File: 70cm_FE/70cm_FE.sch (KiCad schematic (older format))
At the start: 142 parts, among them J2 U.FL, J3 U.FL, J4 U.FL, Q1 2SC3356, Q2 2SC3356, Q3 2SC3356, Q4 2N7002, U1 HT7533-1, U2 74HC14, U3 74HC14, U4 LM393, U5 M68710L

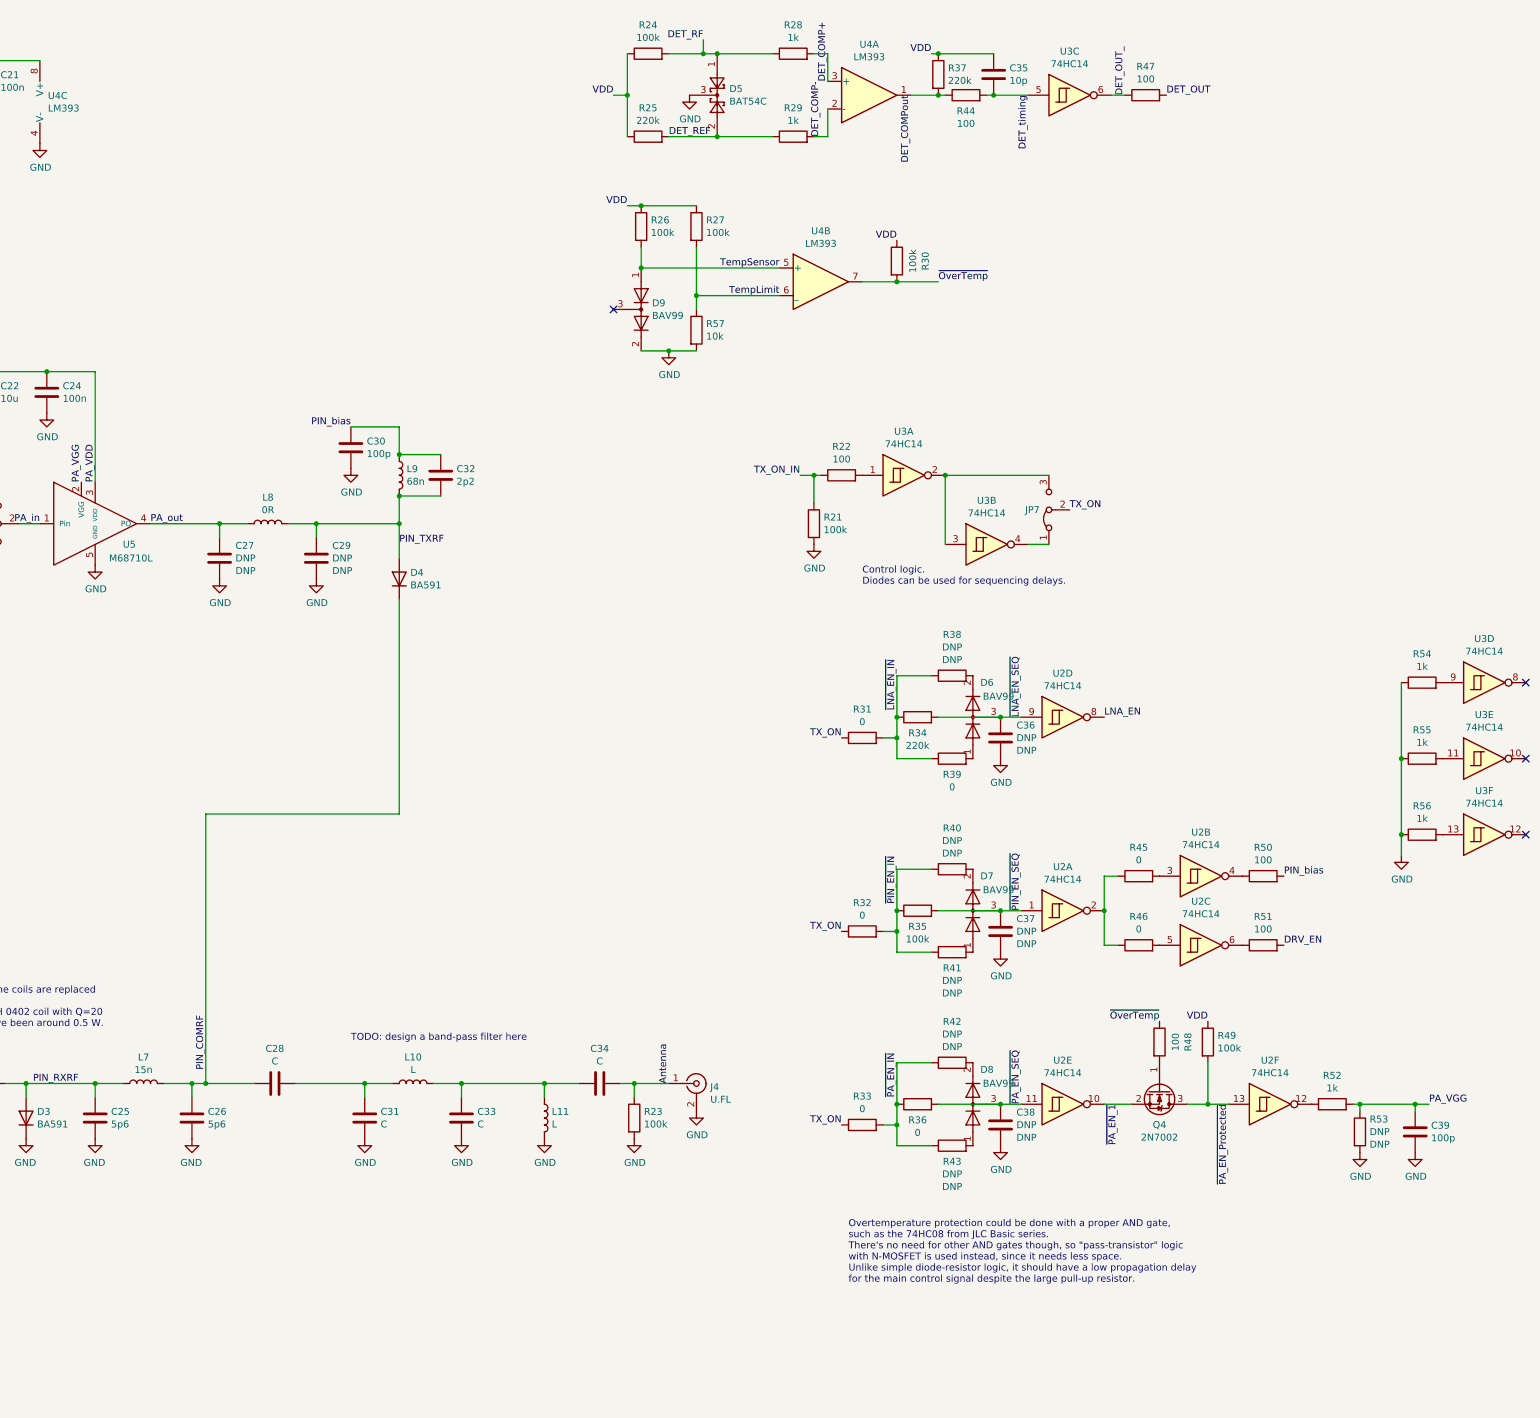
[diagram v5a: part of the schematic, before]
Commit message: Change order of inverters for simpler layout
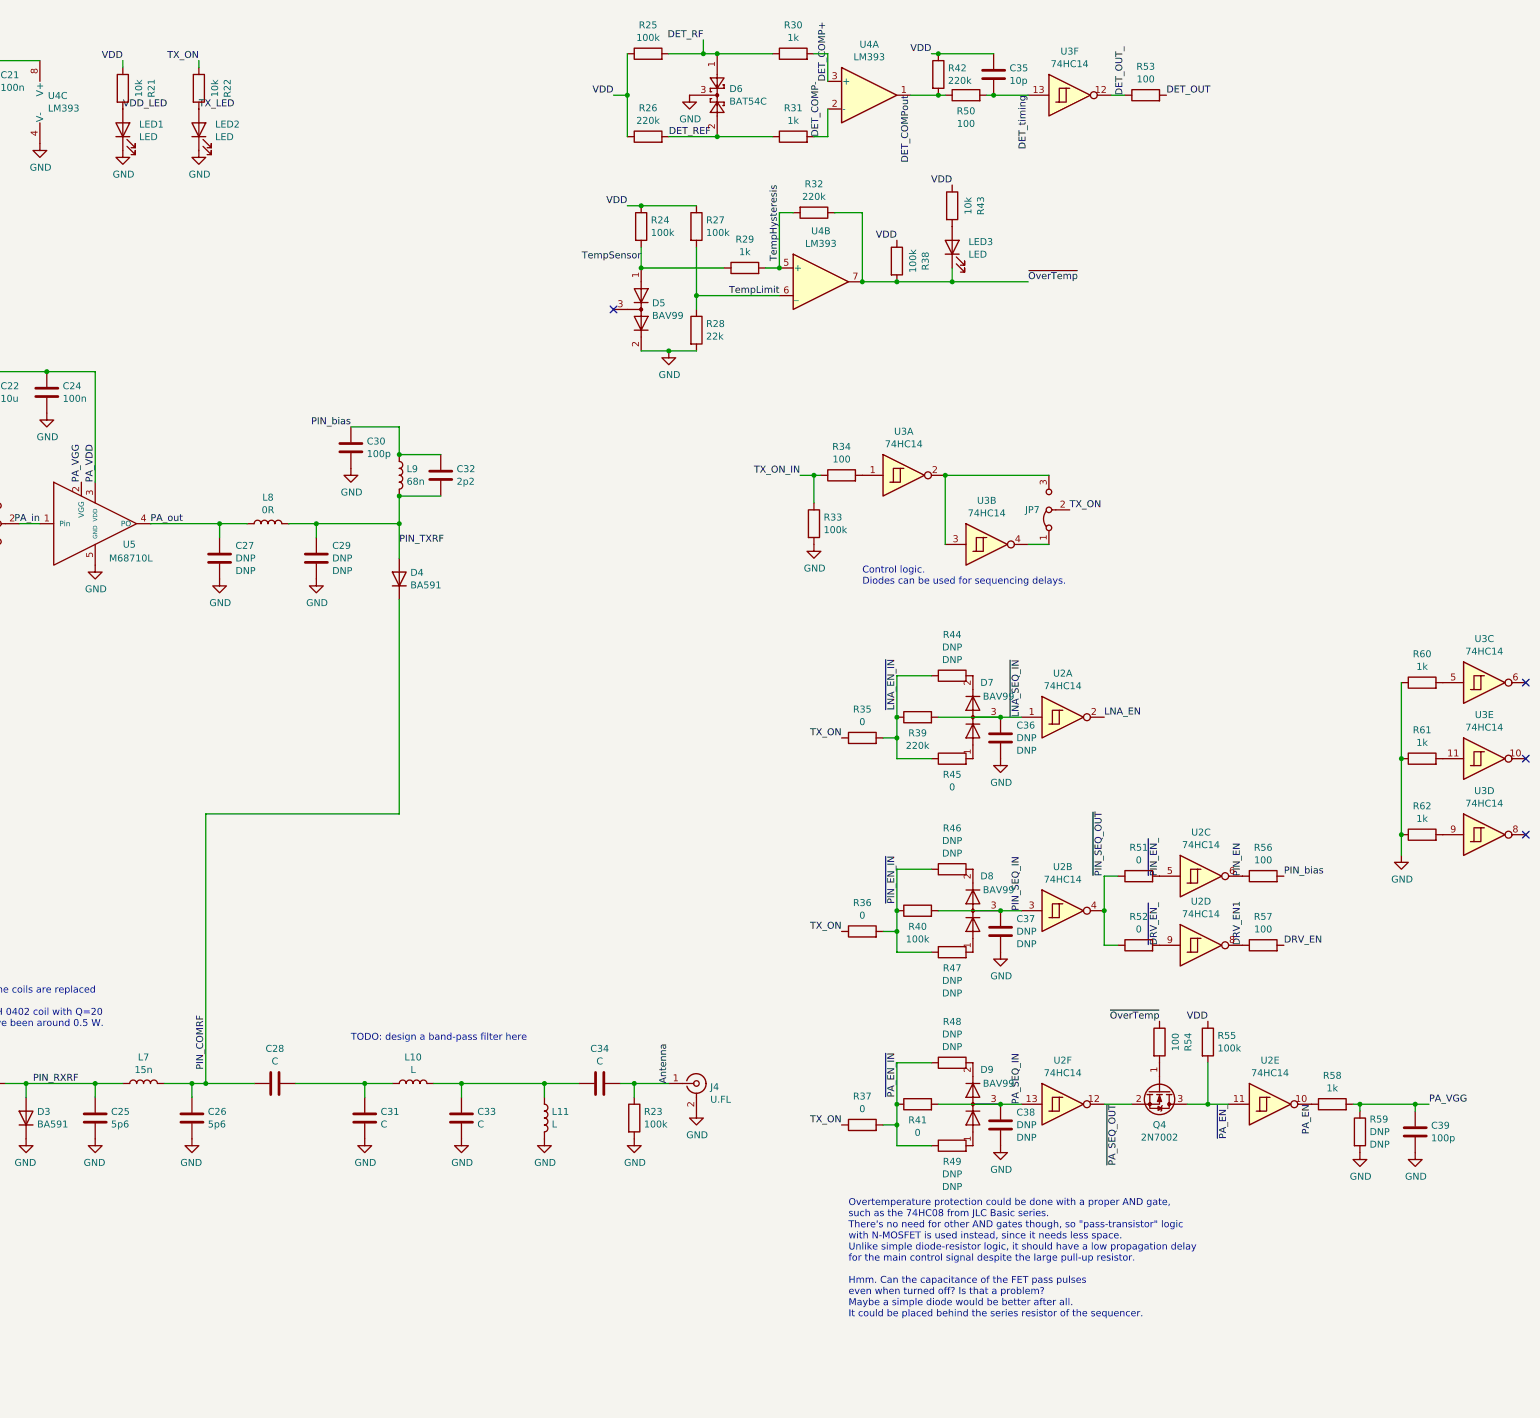
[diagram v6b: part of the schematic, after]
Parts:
- added LED1, LED2, LED3: LED, LED_SMD:LED_0603_1608Metric, symbol Device:LED
- added R21, R22, R43: 10k, Resistor_SMD:R_0402_1005Metric, symbol Device:R
- added R29: 1k, Resistor_SMD:R_0402_1005Metric, symbol Device:R
- added R32: 220k, Resistor_SMD:R_0402_1005Metric, symbol Device:R
- Q4: LCSC (none) -> C8545
- R28: renamed from R57; value 10k -> 22k
- renumbered D9 to D5, D5 to D6, D6 to D7, D7 to D8, D8 to D9, R26 to R24, R24 to R25, R25 to R26, R28 to R30, R29 to R31, R21 to R33, R22 to R34, R31 to R35, R32 to R36, R33 to R37, R30 to R38, R34 to R39, R35 to R40, R36 to R41, R37 to R42, R38 to R44, R39 to R45, R40 to R46, R41 to R47, R42 to R48, R43 to R49, R44 to R50, R45 to R51, R46 to R52, R47 to R53, R48 to R54, R49 to R55, R50 to R56, R51 to R57, R52 to R58, R53 to R59, R54 to R60, R55 to R61, R56 to R62
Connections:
- net DET_OUT_: now also U3.12; no longer U3.6
- net DET_timing: now also U3.13; no longer U3.5
- net GND: now also LED1.1 (K), LED2.1 (K)
- net LNA_EN: now also U2.2; no longer U2.8
- net TX_ON: now also R22.1
- net TempSensor: now also R29.1; no longer U4.5 (+)
- net VDD: now also R21.1, R43.1
- net ~OverTemp~: now also LED3.1 (K), R32.1
- net ~PIN_SEQ_OUT~: now reaches R51.1, R52.1
- net ~PIN_SEQ_OUT~: now also U2.4; no longer U2.2
- net PIN_SEQ_IN: now reaches U2.3
- net PIN_SEQ_IN: now also C37.1, D8.3 (K), R40.2; no longer R51.2
- net PIN_EN: now reaches R56.1
- net PIN_EN: now also U2.6; no longer U2.4
- net PA_EN: now reaches R58.1
- net PA_EN: now also U2.10; no longer U2.12
- net at R60.2: now also U3.5; no longer U3.9
- net at R62.2: now also U3.9; no longer U3.13
- net ~DRV_EN_~: now reaches R52.2
- net ~DRV_EN_~: now also U2.9; no longer U2.5
- net DRV_EN1: now reaches R57.1
- net DRV_EN1: now also U2.8; no longer U2.6
- net ~LNA_EN_SEQ~ renamed ~LNA_SEQ_IN~
- net ~LNA_SEQ_IN~: now also U2.1; no longer U2.9
- net ~PA_EN_1~ renamed ~PA_SEQ_OUT~
- net ~PA_SEQ_OUT~: now also U2.12; no longer U2.10
- net ~PA_EN_Protected~ renamed ~PA_EN_~
- net ~PA_EN_~: now also U2.11; no longer U2.13
- net ~PA_EN_SEQ~ renamed PA_SEQ_IN
- net PA_SEQ_IN: now also U2.13; no longer U2.11
- removed net ~PIN_EN_SEQ~: C37.1, D8.3 (K), R40.2, U2.1
- new net: LED3.2 (A), R43.2
- new net TX_LED: LED2.2 (A), R22.2
- new net TempHysteresis: R29.2, R32.2, U4.5 (+)
- new net VDD_LED: LED1.2 (A), R21.2
- new net ~PIN_EN_~: R51.2, U2.5
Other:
- note added: "Overtemperature protection could be done with a proper AND gate,\nsuch as the 74HC08 from JLC Basic series.\nThere's no need for other AND gates though, so "pass-transistor" logic\nwith N-MOSFET is used instead, since it needs less space.\nUnlike simple diode-resistor logic, it should have a low propagation delay\nfor the main control signal despite the large pull-up resistor.\n\nHmm. Can the cap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"
- note removed: "Overtemperature protection could be done with a proper AND gate,\nsuch as the 74HC08 from JLC Basic series.\nThere's no need for other AND gates though, so "pass-transistor" logic\nwith N-MOSFET is used instead, since it needs less space.\nUnlike simple diode-resistor logic, it should have a low propagation delay\nfor the main control signal despite the large pull-up resistor."
- moved on the sheet: U2A, U2B, U2C, U2D, U2E, U2F, U3C, U3D, U3F
